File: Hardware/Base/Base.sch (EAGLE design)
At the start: 70 parts, among them IC1 74LS245N, T1 2N3904, T10 2N3904, T11 2N3904, T2 2N3904, T3 2N3904, T4 2N3904, T5 2N3904, T6 2N3904, T7 2N3904, T8 2N3904, T9 2N3904

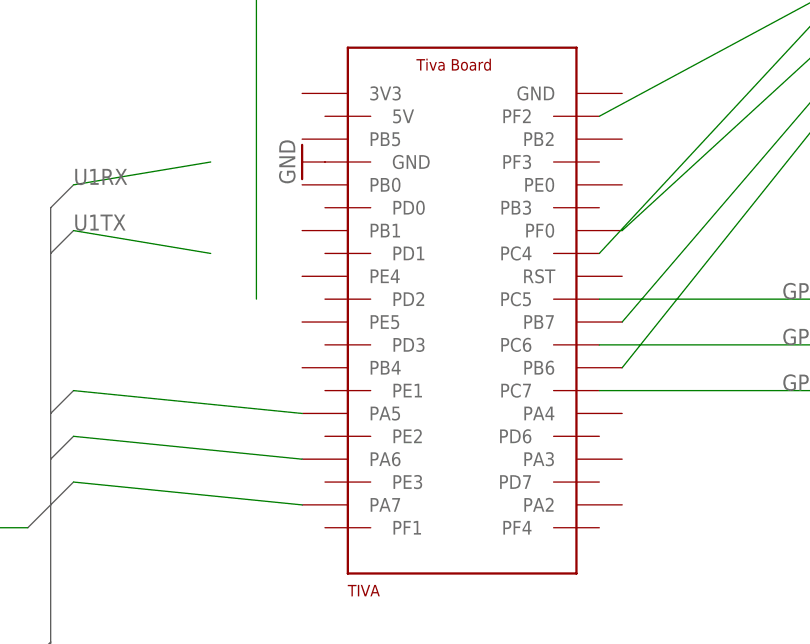
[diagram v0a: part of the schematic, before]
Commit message: Begin Xbee connections.
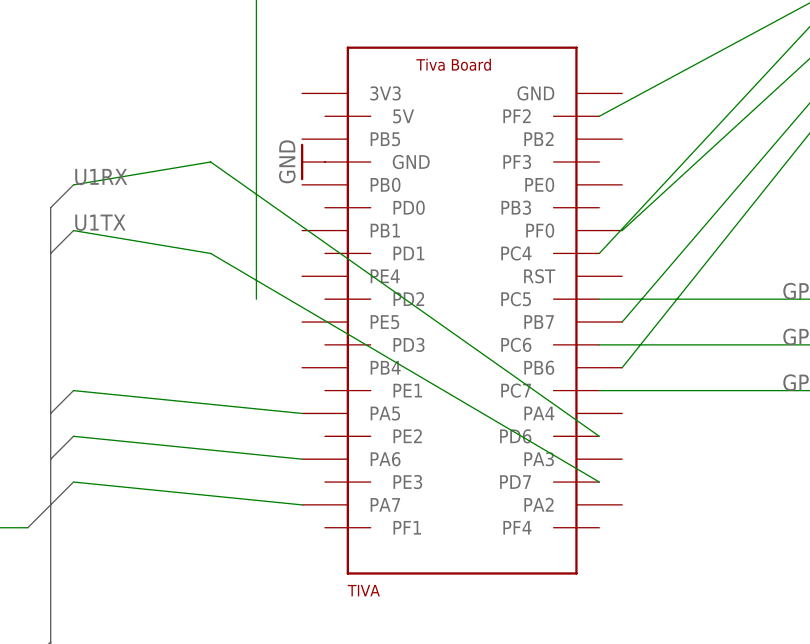
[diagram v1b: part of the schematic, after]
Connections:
- net U1RX: now also TIVA.PD6
- net U1TX: now also TIVA.PD7
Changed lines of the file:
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@@
 <wire x1="-15.24" y1="45.72" x2="-30.48" y2="43.18" width="0.1524" layer="91"/>
 <label x="-30.48" y="43.18" size="1.778" layer="95"/>
+<pinref part="TIVA" gate="TIVA" pin="PD6"/>
+<wire x1="-15.24" y1="45.72" x2="27.94" y2="15.24" width="0.1524" layer="91"/>
 </segment>
 <segment>
@@
 <wire x1="-15.24" y1="35.56" x2="-30.48" y2="38.1" width="0.1524" layer="91"/>
 <label x="-30.48" y="38.1" size="1.778" layer="95"/>
+<pinref part="TIVA" gate="TIVA" pin="PD7"/>
+<wire x1="-15.24" y1="35.56" x2="27.94" y2="10.16" width="0.1524" layer="91"/>
 </segment>
 <segment>

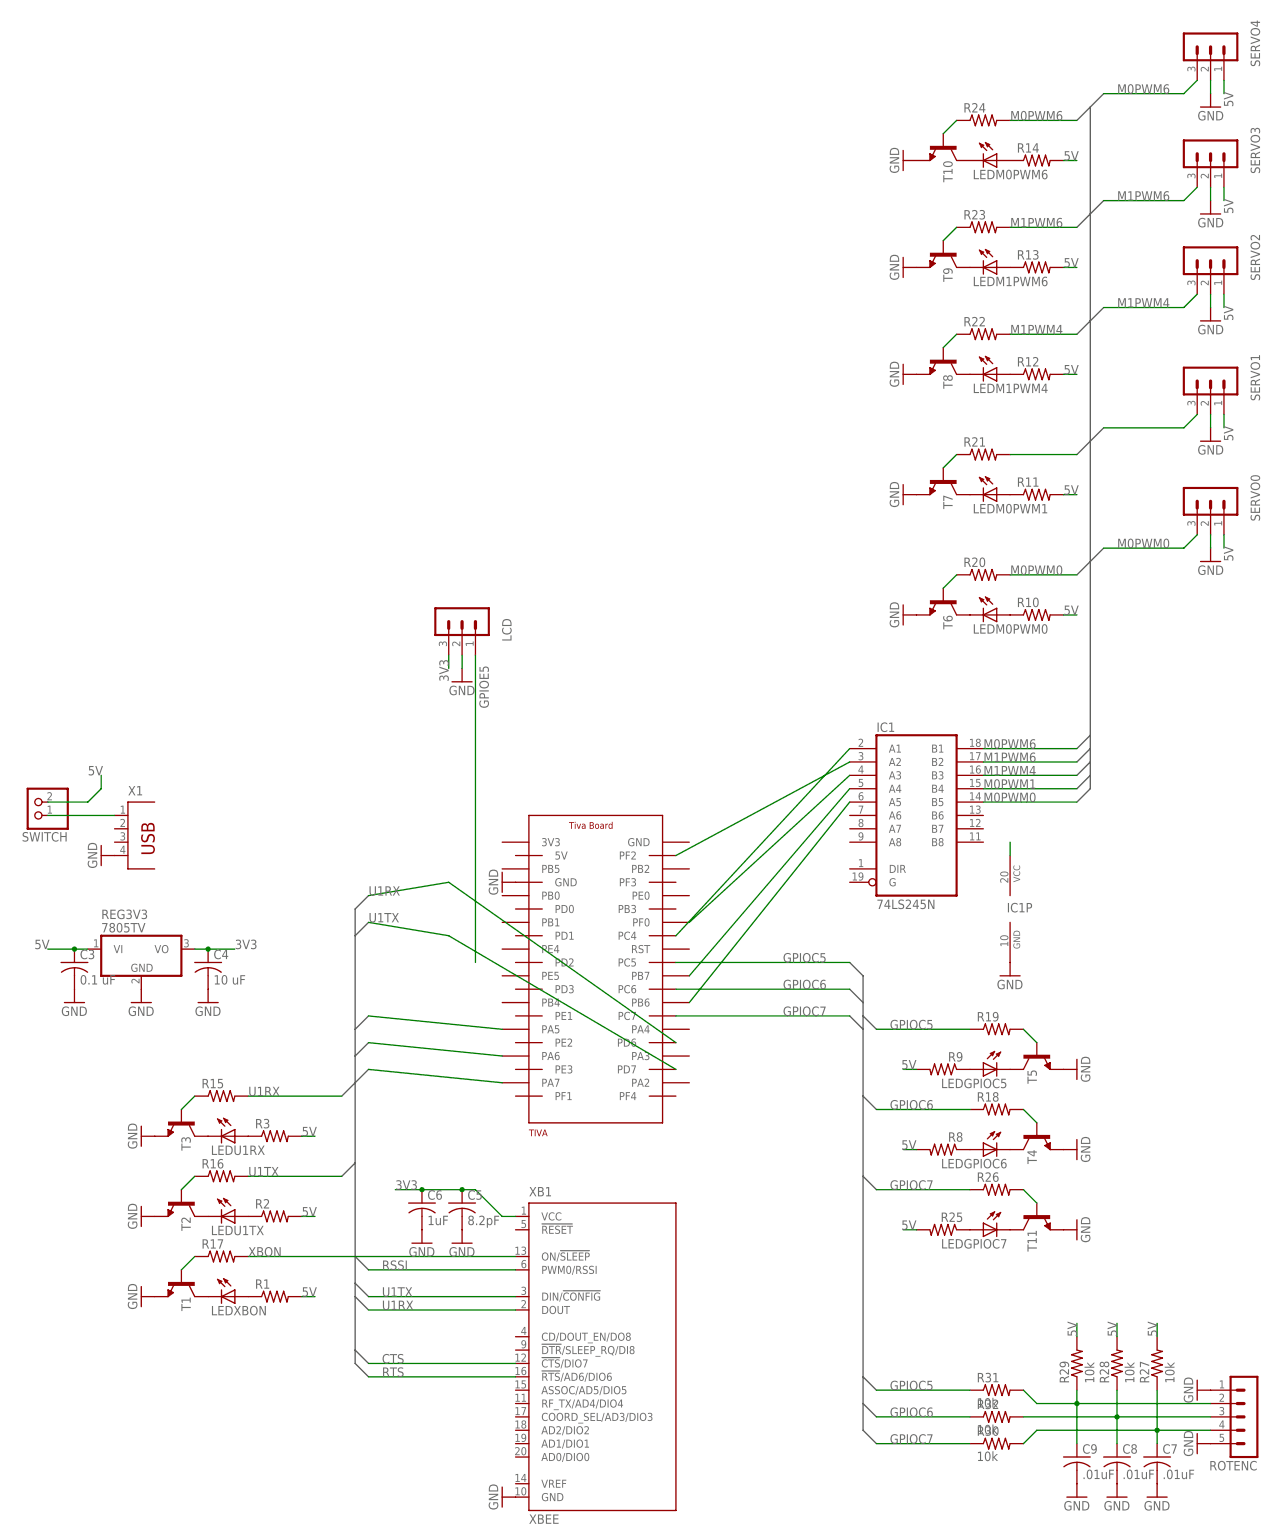
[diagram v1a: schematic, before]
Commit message: No airwires.
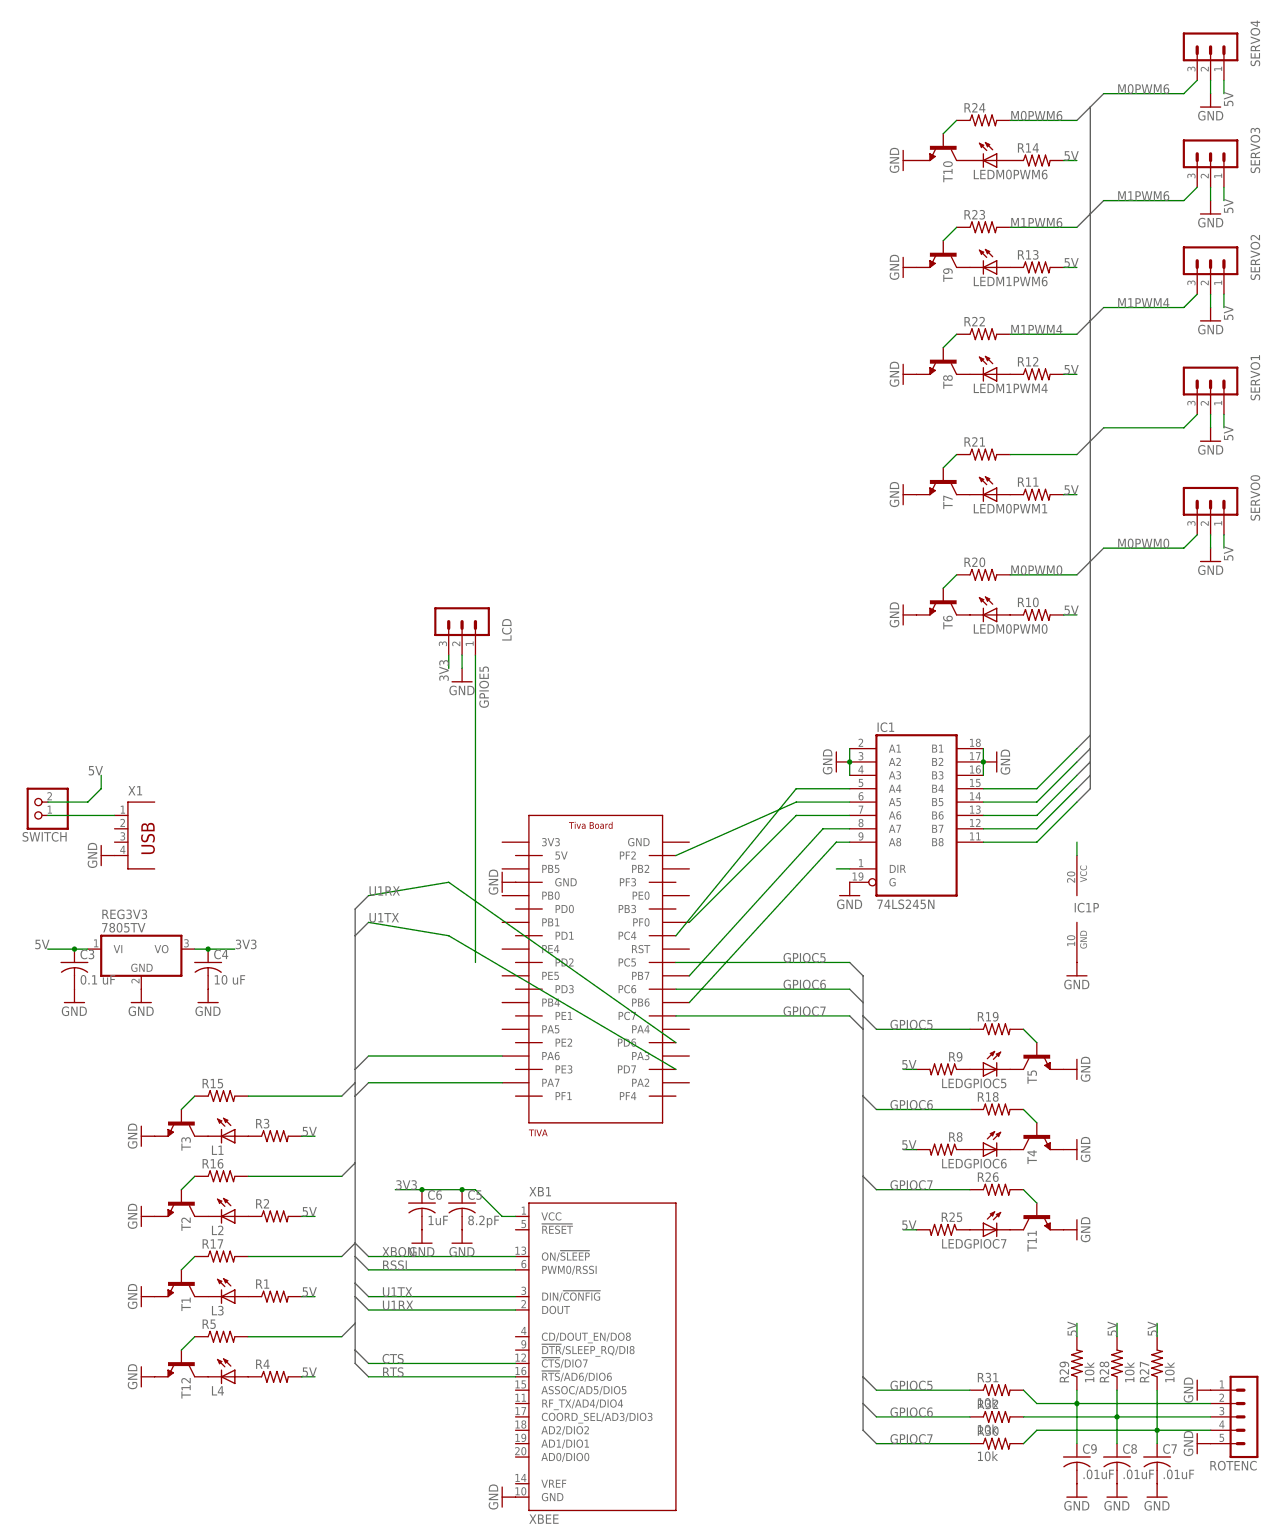
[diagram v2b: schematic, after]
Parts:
- added L4: (no value), led:LED5MM
- added R4, R5: (no value), rcl:R-US_0207/7
- added T12: 2N3904, transistor:2N3904
- renumbered LEDU1RX to L1, LEDU1TX to L2, LEDXBON to L3
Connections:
- new net N$43: L4.C, T12.C
- new net N$44: L4.A, R4.1
- new net N$45: R5.1, T12.B
- net 5V: now also IC1A.DIR, R4.2
- net CTS: now also TIVA.PA6; no longer TIVA.PA5
- net GND: now also IC1A.A1, IC1A.A2, IC1A.A3, IC1A.B1, IC1A.B2, IC1A.B3, IC1A.G, T12.E
- net M0PWM0: now also IC1A.B8; no longer IC1A.B5
- net M0PWM1: now also IC1A.B7; no longer IC1A.B4
- net M0PWM6: now also IC1A.B4; no longer IC1A.B1
- net M1PWM4: now also IC1A.B6; no longer IC1A.B3
- net M1PWM6: now also IC1A.B5; no longer IC1A.B2
- net N$39: now also IC1A.A6; no longer IC1A.A3
- net N$40: now also IC1A.A5; no longer IC1A.A2
- net N$41: now also IC1A.A7; no longer IC1A.A4
- net N$42: now also IC1A.A8; no longer IC1A.A5
- net N$8: now also IC1A.A4; no longer IC1A.A1
- net RSSI: now also R5.2; no longer TIVA.PA7
- net RTS: now also TIVA.PA7; no longer TIVA.PA6
- net U1RX: now also R16.2; no longer R15.2
- net U1TX: now also R17.2; no longer R16.2
- net XBON: now also R15.2; no longer R17.2
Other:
- moved on the sheet: IC1P

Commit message: First printable.
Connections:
- net GPIOE5: now also TIVA.PE5
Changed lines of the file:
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@@
 <grid distance="0.1" unitdist="inch" unit="inch" style="lines" multiple="1" display="no" altdistance="0.01" altunitdist="inch" altunit="inch"/>
 <layers>
-<layer number="1" name="Top" color="4" fill="1" visible="no" active="no"/>
-<layer number="2" name="Route2" color="1" fill="3" visible="no" active="no"/>
-<layer number="3" name="Route3" color="4" fill="3" visible="no" active="no"/>
-<layer number="4" name="Route4" color="1" fill="4" visible="no" active="no"/>
-<layer number="5" name="Route5" color="4" fill="4" visible="no" active="no"/>
-<layer number="6" name="Route6" color="1" fill="8" visible="no" active="no"/>
-<layer number="7" name="Route7" color="4" fill="8" visible="no" active="no"/>
-<layer number="8" name="Route8" color="1" fill="2" visible="no" active="no"/>
-<layer number="9" name="Route9" color="4" fill="2" visible="no" active="no"/>
-<layer number="10" name="Route10" color="1" fill="7" visible="no" active="no"/>
-<layer number="11" name="Route11" color="4" fill="7" visible="no" active="no"/>
-<layer number="12" name="Route12" color="1" fill="5" visible="no" active="no"/>
-<layer number="13" name="Route13" color="4" fill="5" visible="no" active="no"/>
-<layer number="14" name="Route14" color="1" fill="6" visible="no" active="no"/>
-<layer number="15" name="Route15" color="4" fill="6" visible="no" active="no"/>
-<layer number="16" name="Bottom" color="1" fill="1" visible="no" active="no"/>
-<layer number="17" name="Pads" color="2" fill="1" visible="no" active="no"/>
-<layer number="18" name="Vias" color="2" fill="1" visible="no" active="no"/>
-<layer number="19" name="Unrouted" color="6" fill="1" visible="no" active="no"/>
-<layer number="20" name="Dimension" color="15" fill="1" visible="no" active="no"/>
-<layer number="21" name="tPlace" color="7" fill="1" visible="no" active="no"/>
-<layer number="22" name="bPlace" color="7" fill="1" visible="no" active="no"/>
-<layer number="23" name="tOrigins" color="15" fill="1" visible="no" active="no"/>
-<layer number="24" name="bOrigins" color="15" fill="1" visible="no" active="no"/>
-<layer number="25" name="tNames" color="7" fill="1" visible="no" active="no"/>
-<layer number="26" name="bNames" color="7" fill="1" visible="no" active="no"/>
-<layer number="27" name="tValues" color="7" fill="1" visible="no" active="no"/>
-<layer number="28" name="bValues" color="7" fill="1" visible="no" active="no"/>
+<layer number="1" name="Top" color="4" fill="1" visible="yes" active="no"/>
+<layer number="2" name="Route2" color="1" fill="3" visible="yes" active="no"/>
+<layer number="3" name="Route3" color="4" fill="3" visible="yes" active="no"/>
+<layer number="4" name="Route4" color="1" fill="4" visible="yes" active="no"/>
+<layer number="5" name="Route5" color="4" fill="4" visible="yes" active="no"/>
+<layer number="6" name="Route6" color="1" fill="8" visible="yes" active="no"/>
+<layer number="7" name="Route7" color="4" fill="8" visible="yes" active="no"/>
+<layer number="8" name="Route8" color="1" fill="2" visible="yes" active="no"/>
+<layer number="9" name="Route9" color="4" fill="2" visible="yes" active="no"/>
+<layer number="10" name="Route10" color="1" fill="7" visible="yes" active="no"/>
+<layer number="11" name="Route11" color="4" fill="7" visible="yes" active="no"/>
+<layer number="12" name="Route12" color="1" fill="5" visible="yes" active="no"/>
+<layer number="13" name="Route13" color="4" fill="5" visible="yes" active="no"/>
+<layer number="14" name="Route14" color="1" fill="6" visible="yes" active="no"/>
+<layer number="15" name="Route15" color="4" fill="6" visible="yes" active="no"/>
+<layer number="16" name="Bottom" color="1" fill="1" visible="yes" active="no"/>
+<layer number="17" name="Pads" color="2" fill="1" visible="yes" active="no"/>
+<layer number="18" name="Vias" color="2" fill="1" visible="yes" active="no"/>
+<layer number="19" name="Unrouted" color="6" fill="1" visible="yes" active="no"/>
+<layer number="20" name="Dimension" color="15" fill="1" visible="yes" active="no"/>
+<layer number="21" name="tPlace" color="7" fill="1" visible="yes" active="no"/>
+<layer number="22" name="bPlace" color="7" fill="1" visible="yes" active="no"/>
+<layer number="23" name="tOrigins" color="15" fill="1" visible="yes" active="no"/>
+<layer number="24" name="bOrigins" color="15" fill="1" visible="yes" active="no"/>
+<layer number="25" name="tNames" color="7" fill="1" visible="yes" active="no"/>
+<layer number="26" name="bNames" color="7" fill="1" visible="yes" active="no"/>
+<layer number="27" name="tValues" color="7" fill="1" visible="yes" active="no"/>
+<layer number="28" name="bValues" color="7" fill="1" visible="yes" active="no"/>
 <layer number="29" name="tStop" color="7" fill="3" visible="no" active="no"/>
 <layer number="30" name="bStop" color="7" fill="6" visible="no" active="no"/>
@@
 <layer number="35" name="tGlue" color="7" fill="4" visible="no" active="no"/>
 <layer number="36" name="bGlue" color="7" fill="5" visible="no" active="no"/>
-<layer number="37" name="tTest" color="7" fill="1" visible="no" active="no"/>
-<layer number="38" name="bTest" color="7" fill="1" visible="no" active="no"/>
+<layer number="37" name="tTest" color="7" fill="1" visible="yes" active="no"/>
+<layer number="38" name="bTest" color="7" fill="1" visible="yes" active="no"/>
 <layer number="39" name="tKeepout" color="4" fill="11" visible="no" active="no"/>
 <layer number="40" name="bKeepout" color="1" fill="11" visible="no" active="no"/>
@@
 <layer number="44" name="Drills" color="7" fill="1" visible="no" active="no"/>
 <layer number="45" name="Holes" color="7" fill="1" visible="no" active="no"/>
-<layer number="46" name="Milling" color="3" fill="1" visible="no" active="no"/>
-<layer number="47" name="Measures" color="7" fill="1" visible="no" active="no"/>
-<layer number="48" name="Document" color="7" fill="1" visible="no" active="no"/>
-<layer number="49" name="Reference" color="7" fill="1" visible="no" active="no"/>
-<layer number="50" name="dxf" color="7" fill="1" visible="no" active="no"/>
-<layer number="51" name="tDocu" color="7" fill="1" visible="no" active="no"/>
-<layer number="52" name="bDocu" color="7" fill="1" visible="no" active="no"/>
-<layer number="53" name="tGND_GNDA" color="7" fill="9" visible="no" active="no"/>
-<layer number="54" name="bGND_GNDA" color="1" fill="9" visible="no" active="no"/>
-<layer number="56" name="wert" color="7" fill="1" visible="no" active="no"/>
-<layer number="57" name="tCAD" color="7" fill="1" visible="no" active="no"/>
-<layer number="59" name="tCarbon" color="7" fill="1" visible="no" active="no"/>
-<layer number="60" name="bCarbon" color="7" fill="1" visible="no" active="no"/>
+<layer number="46" name="Milling" color="3" fill="1" visible="yes" active="no"/>
+<layer number="47" name="Measures" color="7" fill="1" visible="yes" active="no"/>
+<layer number="48" name="Document" color="7" fill="1" visible="yes" active="no"/>
+<layer number="49" name="Reference" color="7" fill="1" visible="yes" active="no"/>
+<layer number="50" name="dxf" color="7" fill="1" visible="yes" active="no"/>
+<layer number="51" name="tDocu" color="7" fill="1" visible="yes" active="no"/>
+<layer number="52" name="bDocu" color="7" fill="1" visible="yes" active="no"/>
+<layer number="53" name="tGND_GNDA" color="7" fill="9" visible="yes" active="no"/>
+<layer number="54" name="bGND_GNDA" color="1" fill="9" visible="yes" active="no"/>
+<layer number="56" name="wert" color="7" fill="1" visible="yes" active="no"/>
+<layer number="57" name="tCAD" color="7" fill="1" visible="yes" active="no"/>
+<layer number="59" name="tCarbon" color="7" fill="1" visible="yes" active="no"/>
+<layer number="60" name="bCarbon" color="7" fill="1" visible="yes" active="no"/>
 <layer number="90" name="Modules" color="5" fill="1" visible="yes" active="yes"/>
 <layer number="91" name="Nets" color="2" fill="1" visible="yes" active="yes"/>
@@
 <pinref part="LCD" gate="G$1" pin="1"/>
 <label x="-7.62" y="78.74" size="1.778" layer="95" rot="R90"/>
-</segment>
-</net>
+<pinref part="TIVA" gate="TIVA" pin="PE5"/>
+<wire x1="-10.16" y1="30.48" x2="-5.08" y2="27.94" width="0.1524" layer="91"/>
+</segment>
+</net>
